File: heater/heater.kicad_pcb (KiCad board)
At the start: 2 copper layers, 60 x 74 mm, 3 parts

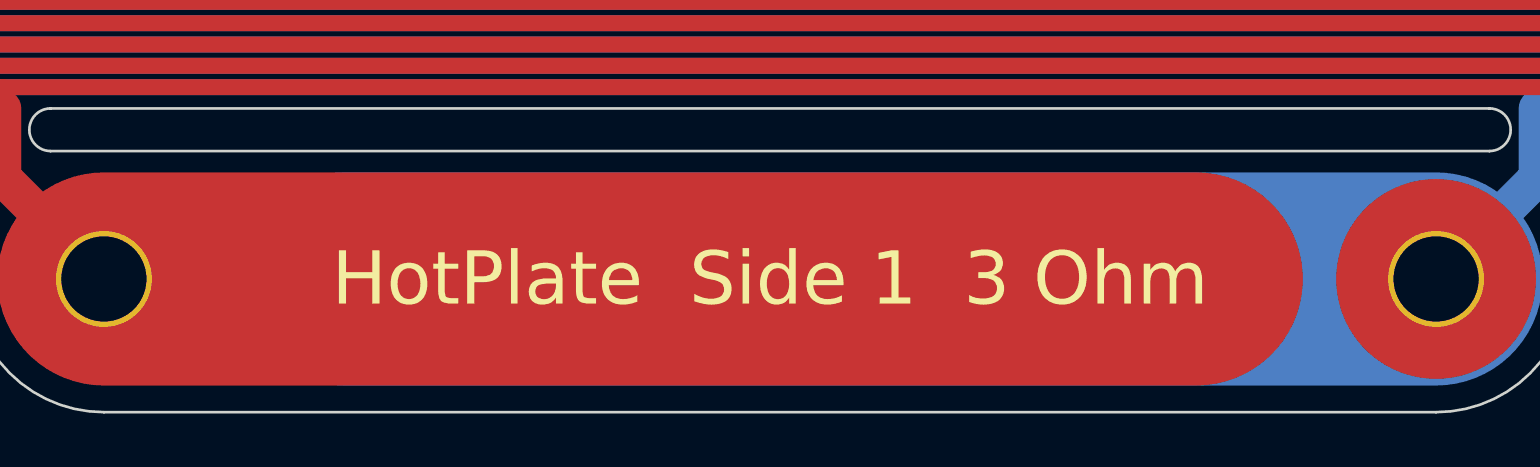
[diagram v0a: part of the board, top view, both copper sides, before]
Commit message: Support Fahrenheit display Fix silkscreen on heater
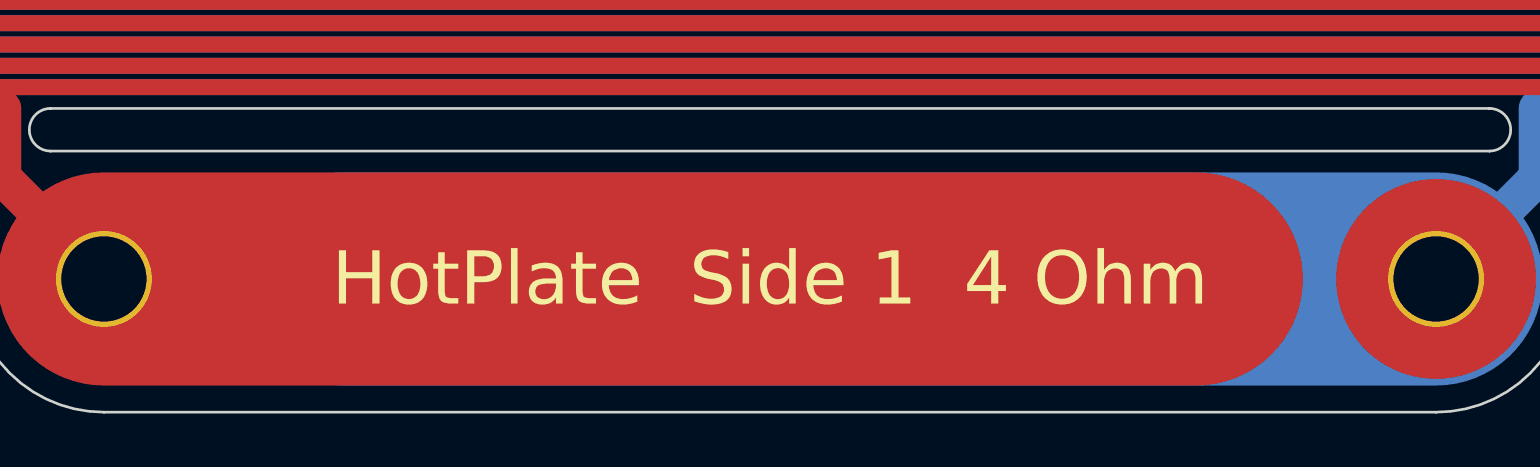
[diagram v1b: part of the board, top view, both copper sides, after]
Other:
- board text added: "HotPlate Side 1 4 Ohm"
- board text added: "HotPlate Side 2 4 Ohm"
- board text removed: "HotPlate Side 1 3 Ohm"
- board text removed: "HotPlate Side 2 3 Ohm"
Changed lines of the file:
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@@
   (gr_arc (start 155 38) (mid 158.535534 39.464466) (end 160 43) (layer "Edge.Cuts") (width 0.1))
   (gr_line (start 105 38) (end 155 38) (layer "Edge.Cuts") (width 0.1))
-  (gr_text "HotPlate  Side 2  3 Ohm" (at 130 107) (layer "B.SilkS")
+  (gr_text "HotPlate  Side 2  4 Ohm" (at 130 107) (layer "B.SilkS")
     (effects (font (size 2 2) (thickness 0.3)) (justify mirror))
   )
-  (gr_text "HotPlate  Side 1  3 Ohm" (at 130 107) (layer "F.SilkS")
+  (gr_text "HotPlate  Side 1  4 Ohm" (at 130 107) (layer "F.SilkS")
     (effects (font (size 2 2) (thickness 0.3)))
   )

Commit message: Change text on heater plate
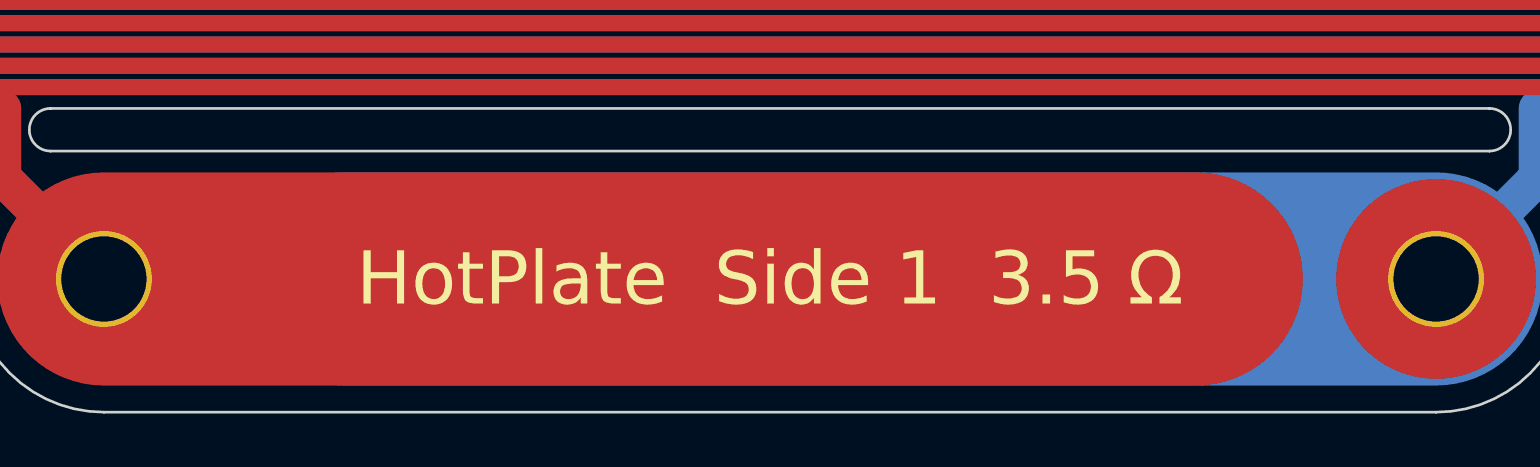
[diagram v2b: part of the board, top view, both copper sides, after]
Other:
- board text added: "HotPlate Side 1 3.5 Ω"
- board text added: "HotPlate Side 2 3.5 Ω"
- board text removed: "HotPlate Side 1 4 Ohm"
- board text removed: "HotPlate Side 2 4 Ohm"
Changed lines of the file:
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@@
   (title_block
     (title "Heater")
-    (rev "1")
+    (rev "2")
   )
   (layers
@@
   (gr_arc (start 155 38) (mid 158.535534 39.464466) (end 160 43) (layer "Edge.Cuts") (width 0.1))
   (gr_line (start 105 38) (end 155 38) (layer "Edge.Cuts") (width 0.1))
-  (gr_text "HotPlate  Side 2  4 Ohm" (at 130 107) (layer "B.SilkS")
+  (gr_text "HotPlate  Side 2  3.5 Ω" (at 130 107) (layer "B.SilkS")
     (effects (font (size 2 2) (thickness 0.3)) (justify mirror))
   )
-  (gr_text "HotPlate  Side 1  4 Ohm" (at 130 107) (layer "F.SilkS")
+  (gr_text "HotPlate  Side 1  3.5 Ω" (at 130 107) (layer "F.SilkS")
     (effects (font (size 2 2) (thickness 0.3)))
   )
